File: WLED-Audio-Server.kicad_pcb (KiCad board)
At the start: 2 copper layers, 70 x 50 mm, 25 parts, among them J1 AudioJack4, J2 AudioJack4, SW1 SW_Push, U1 LMV358, U2 ESP32-DEVKIT-V1

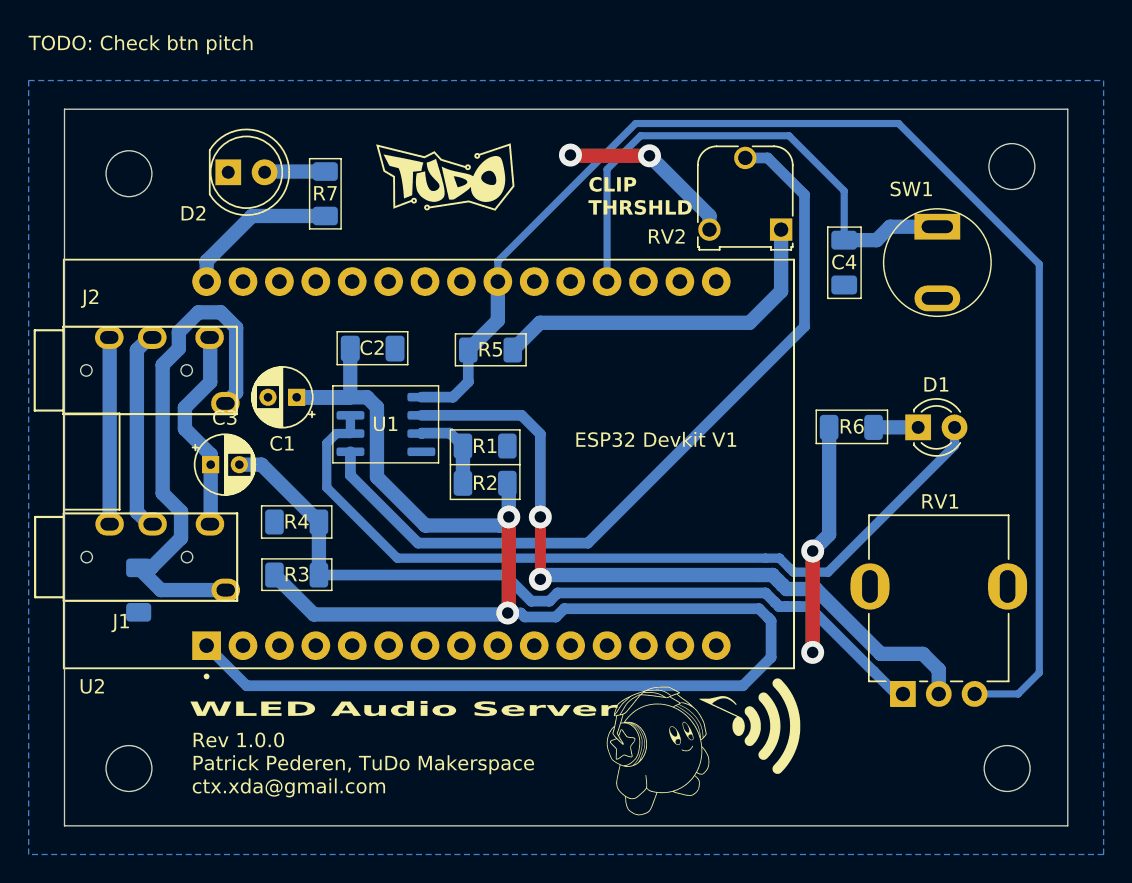
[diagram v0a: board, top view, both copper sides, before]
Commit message: Re-aligned mounting holes
Signed-off-by: Patrick Pedersen <ctx.xda@gmail.com>
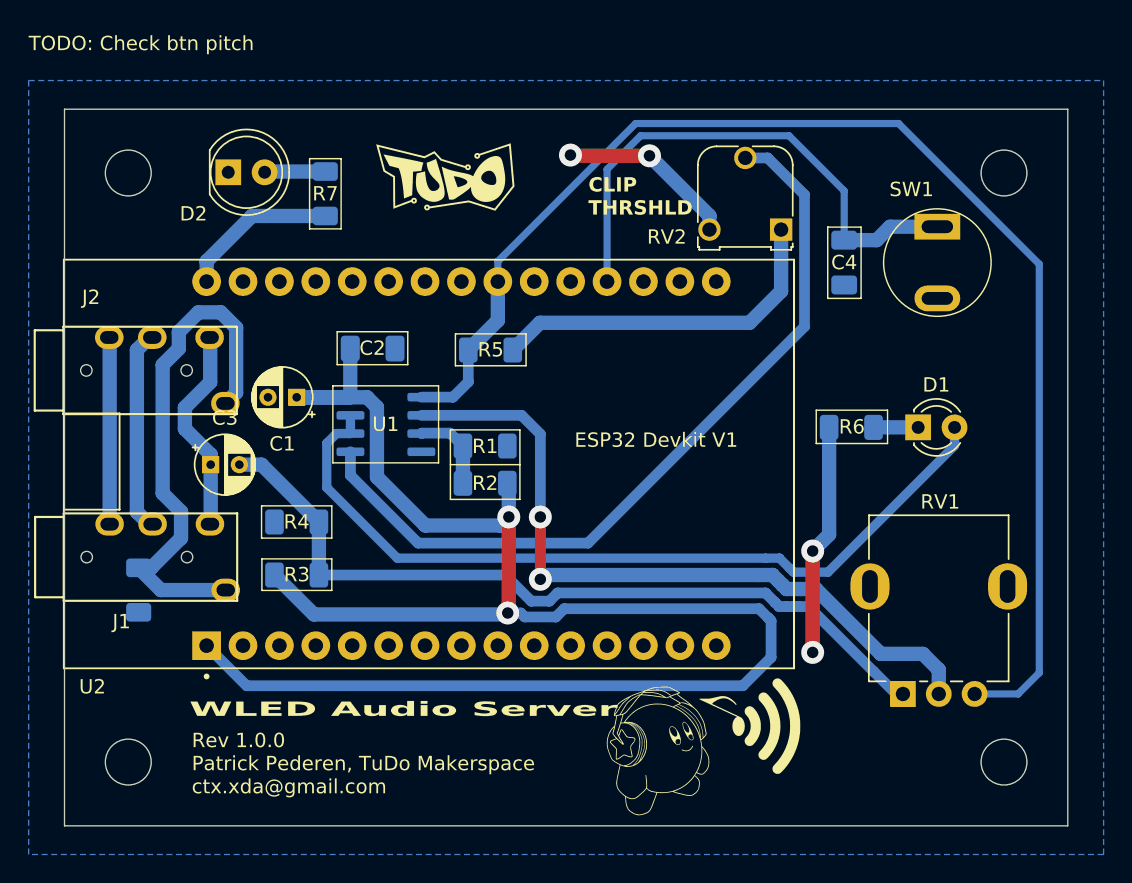
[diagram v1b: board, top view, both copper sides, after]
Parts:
- moved H3 0.71 mm to (156.1, 99.5)
- moved H1 0.50 mm to (156.1, 140.6)
- moved H4 0.45 mm to (95.0, 140.6)
- moved H2 0.07 mm to (95.0, 99.5)
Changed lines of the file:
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@@
 	(footprint "MountingHole:MountingHole_3.2mm_M3"
 		(layer "F.Cu")
-		(at 95 141)
+		(at 94.95 140.55)
 		(descr "Mounting Hole 3.2mm, no annular, M3")
 		(tags "mounting hole 3.2mm no annular m3")
@@
 	(footprint "MountingHole:MountingHole_3.2mm_M3"
 		(layer "F.Cu")
-		(at 156.27 141)
+		(at 156.05 140.55)
 		(descr "Mounting Hole 3.2mm, no annular, M3")
 		(tags "mounting hole 3.2mm no annular m3")
@@
 	(footprint "MountingHole:MountingHole_3.2mm_M3"
 		(layer "F.Cu")
-		(at 156.6 99)
+		(at 156.05 99.45)
 		(descr "Mounting Hole 3.2mm, no annular, M3")
 		(tags "mounting hole 3.2mm no annular m3")
@@
 	(footprint "MountingHole:MountingHole_3.2mm_M3"
 		(layer "F.Cu")
-		(at 95 99.5)
+		(at 94.95 99.45)
 		(descr "Mounting Hole 3.2mm, no annular, M3")
 		(tags "mounting hole 3.2mm no annular m3")
@@
 	)
 	(segment
-		(start 120.735 105.613287)
-		(end 130.348287 96)
+		(start 158.511 134.325)
+		(end 157.036 135.8)
 		(width 0.5)
 		(layer "B.Cu")
@@
 	)
 	(segment
-		(start 158.511 134.325)
-		(end 157.036 135.8)
+		(start 158.511 105.811)
+		(end 158.511 134.325)
+		(width 0.5)
+		(layer "B.Cu")
+		(net 33)
+	)
+	(segment
+		(start 157.036 135.8)
+		(end 154 135.8)
+		(width 0.5)
+		(layer "B.Cu")
+		(net 33)
+	)
+	(segment
+		(start 120.735 107.0275)
+		(end 120.735 105.613287)
 		(width 0.5)
 		(layer "B.Cu")
@@
 	)
 	(segment
-		(start 130.348287 96)
-		(end 148.7 96)
-		(width 0.5)
-		(layer "B.Cu")
-		(net 33)
-	)
-	(segment
 		(start 115.4 115.09)
 		(end 117.61 115.09)
@@
 	)
 	(segment
-		(start 120.735 107.0275)
-		(end 120.735 105.613287)
-		(width 0.5)
-		(layer "B.Cu")
-		(net 33)
-	)
-	(segment
-		(start 158.511 105.811)
-		(end 158.511 134.325)
+		(start 130.348287 96)
+		(end 148.7 96)
 		(width 0.5)
 		(layer "B.Cu")
@@
 	)
 	(segment
-		(start 157.036 135.8)
-		(end 154 135.8)
+		(start 120.735 105.613287)
+		(end 130.348287 96)
 		(width 0.5)
 		(layer "B.Cu")

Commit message: Revision 1.0.1: Fixed potentiometer orientation + PB Pitch
Signed-off-by: Patrick Pedersen <ctx.xda@gmail.com>
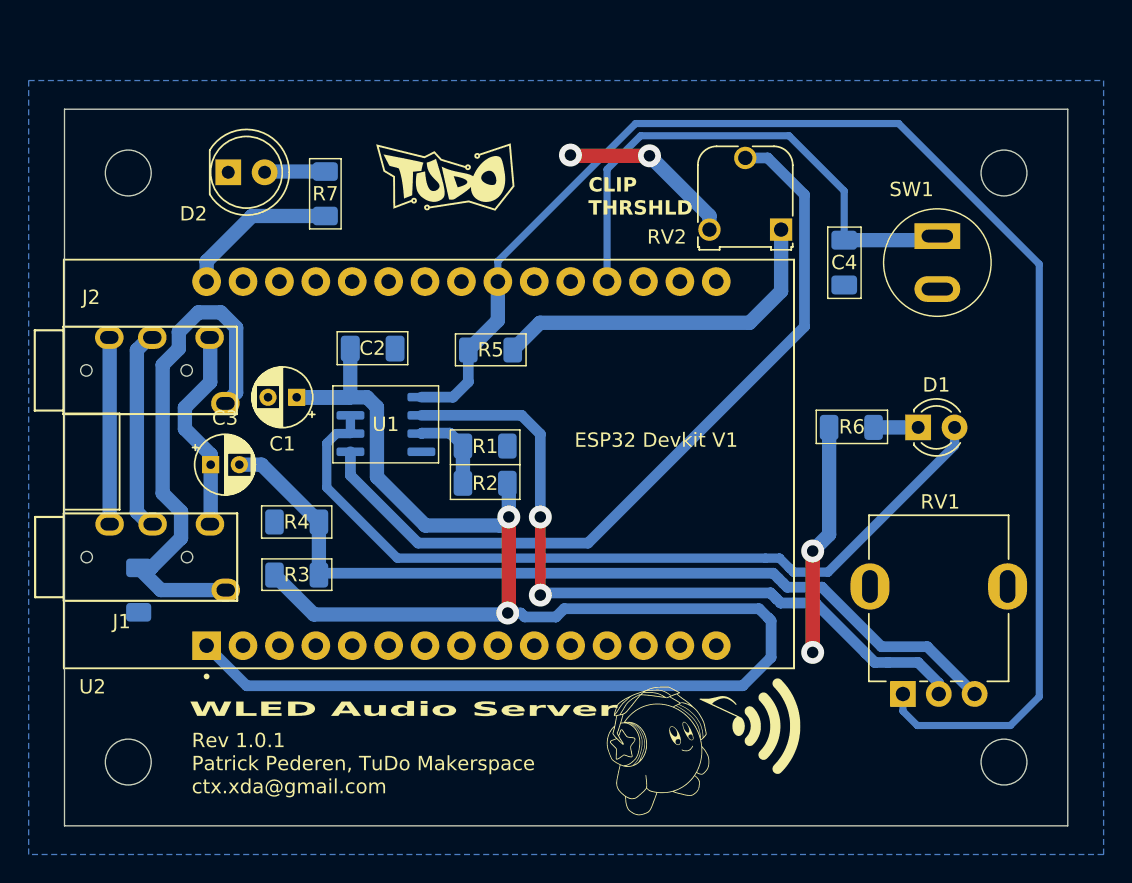
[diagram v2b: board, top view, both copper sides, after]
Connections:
- RV1 pad 1: /Biased at 1.65v -> AUDIO
- RV1 pad 3: AUDIO -> /Biased at 1.65v
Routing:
- net AUDIO: track 92.4 -> 101.4 mm
- net /Biased at 1.65v: track 55.6 -> 60.2 mm
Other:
- board text added: "Rev 1.0.1 Patrick Pederen, TuDo Makerspace ctx.xda@gmail.com"
- board text removed: "Rev 1.0.0 Patrick Pederen, TuDo Makerspace ctx.xda@gmail.com"
- board text removed: "TODO: Check btn pitch"
